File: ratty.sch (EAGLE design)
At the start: 90 parts, among them IC2 L293DD, Q1 BS170, Q2 BS170, Q3 BS170, Q5 BS170, U1 ITG-32001:1

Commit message: latest changes
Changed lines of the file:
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@@
 <part name="S1" library="switch-ck" deviceset="L101-XX-X-MS" device=""/>
 <part name="AGND9" library="supply1" deviceset="AGND" device=""/>
-<part name="GND28" library="supply2" deviceset="DGND" device=""/>
 <part name="GND30" library="supply2" deviceset="DGND" device=""/>
 <part name="GND31" library="supply2" deviceset="DGND" device=""/>
@@
 <part name="SUPPLY1" library="supply2" deviceset="DGND" device=""/>
 <part name="SUPPLY2" library="supply2" deviceset="DGND" device=""/>
+<part name="SUPPLY3" library="supply2" deviceset="DGND" device=""/>
 </parts>
 <sheets>
@@
 <instance part="S1" gate="G$1" x="43.18" y="114.3" rot="R90"/>
 <instance part="AGND9" gate="VR1" x="-93.98" y="213.36"/>
-<instance part="GND28" gate="G$1" x="-88.9" y="157.48"/>
 <instance part="GND30" gate="G$1" x="-50.8" y="157.48"/>
 <instance part="GND31" gate="G$1" x="-33.02" y="157.48"/>
@@
 <instance part="SUPPLY1" gate="G$1" x="30.48" y="53.34" rot="R270"/>
 <instance part="SUPPLY2" gate="G$1" x="-68.58" y="154.94"/>
+<instance part="SUPPLY3" gate="G$1" x="-88.9" y="154.94"/>
 </instances>
 <busses>
@@
 </segment>
 <segment>
-<pinref part="C11" gate="G$1" pin="2"/>
-<wire x1="-88.9" y1="167.64" x2="-88.9" y2="160.02" width="0.1524" layer="91"/>
-<pinref part="GND28" gate="G$1" pin="DGND"/>
-</segment>
-<segment>
 <pinref part="C17" gate="G$1" pin="2"/>
 <pinref part="GND30" gate="G$1" pin="DGND"/>
@@
 <pinref part="SUPPLY2" gate="G$1" pin="DGND"/>
 </segment>
-</net>
+<segment>
+<pinref part="C11" gate="G$1" pin="2"/>
+<wire x1="-88.9" y1="167.64" x2="-88.9" y2="157.48" width="0.1524" layer="91"/>
+<pinref part="SUPPLY3" gate="G$1" pin="DGND"/>
+</segment>
+</net>

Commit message: Changed schematic a bit to make it easier to route
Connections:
- removed net PA_0_ENCODER1_1: U$4.PA0-TIM2_CH1/TIM2_ET/TIM5_CH1, U$8.L_CHA
- removed net PA_1_ENCODER1_2: U$4.PA1-TIM2_CH2/TIM5_CH2/SPI4_MOSI/I2S4_SD, U$8.L_CHB
- removed net PA_5_ENCODER2_1: U$4.PA5-TIM2_CH1/TIM2_ET/SPI1_SCK/I2S1_CK, U$8.R_CHA
- removed net PB3_ENCODER2_2: U$4.PB3-JTDO-SWO/TIME2_CH2/SPI1_SCK/SPI3_SCK/USART1_RX/I2C2_SDA, U$8.R_CHB
- removed net PB7_I2CSDA_FOR_GYRO: U$4.PB7-TIM4_CH2/I2C1_SDA/USART1_RX/SDIO_D0, U1.SDA
- removed net PB8_I2C1SCL_FOR_GYRO: U$4.PB8-TIM4_CH3/TIM10_CH1/I2C1_SCL/SPI5_MOSI/I2C3_SDA, U1.SCL
- removed net PB9_GYROCLK: U$4.PB9-TIM4_CH4/TIM11_CH11/I2C1_SDA/SPI2_NSS/I2C2_SDA, U1.CLKIN
- new net ENCODER1_1: U$4.PA5-TIM2_CH1/TIM2_ET/SPI1_SCK/I2S1_CK, U$8.L_CHA
- new net ENCODER1_2: U$4.PB3-JTDO-SWO/TIME2_CH2/SPI1_SCK/SPI3_SCK/USART1_RX/I2C2_SDA, U$8.L_CHB
- new net ENCODER2_1: U$4.PA0-TIM2_CH1/TIM2_ET/TIM5_CH1, U$8.R_CHA
- new net ENCODER2_2: U$4.PA1-TIM2_CH2/TIM5_CH2/SPI4_MOSI/I2S4_SD, U$8.R_CHB
- new net GYROCLK: U$4.PA9-TIM1_CH2/I2C3_SMBA/USART1_TX/SDIO_D2, U1.CLKIN
- new net I2CSCL_FOR_GYRO: U$4.PA8-MCO_1/TIM1_CH1/I2C3_SCL/USART1_CK/SDIO_D1, U1.SCL
- new net I2CSDA_FOR_GYRO: U$4.PC9-MCO_2/TIM3)CH4/I2C3_SDA/SDIO_D1, U1.SDA
- net L_DIGITAL_IN_1: now also U$4.PB7-TIM4_CH2/I2C1_SDA/USART1_RX/SDIO_D0; no longer U$4.PA8-MCO_1/TIM1_CH1/I2C3_SCL/USART1_CK/SDIO_D1
- net L_DIGITAL_IN_2: now also U$4.PB8-TIM4_CH3/TIM10_CH1/I2C1_SCL/SPI5_MOSI/I2C3_SDA; no longer U$4.PA9-TIM1_CH2/I2C3_SMBA/USART1_TX/SDIO_D2
- net PC9_REC_CIRCUIT_4: now also U$4.PC12-SPI3_MOSI/I2S3_SD/SDIO_CK; no longer U$4.PC9-MCO_2/TIM3)CH4/I2C3_SDA/SDIO_D1
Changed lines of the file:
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@@
 </segment>
 <segment>
-<pinref part="U$4" gate="G$1" pin="PA9-TIM1_CH2/I2C3_SMBA/USART1_TX/SDIO_D2"/>
-<wire x1="200.66" y1="307.34" x2="210.82" y2="307.34" width="0.1524" layer="91"/>
-<label x="210.82" y="307.34" size="1.778" layer="95" xref="yes"/>
+<pinref part="U$4" gate="G$1" pin="PB8-TIM4_CH3/TIM10_CH1/I2C1_SCL/SPI5_MOSI/I2C3_SDA"/>
+<wire x1="200.66" y1="264.16" x2="205.74" y2="264.16" width="0.1524" layer="91"/>
+<label x="205.74" y="264.16" size="1.778" layer="95" xref="yes"/>
 </segment>
 </net>
@@
 </segment>
 <segment>
-<pinref part="U$4" gate="G$1" pin="PA8-MCO_1/TIM1_CH1/I2C3_SCL/USART1_CK/SDIO_D1"/>
-<wire x1="200.66" y1="309.88" x2="210.82" y2="309.88" width="0.1524" layer="91"/>
-<label x="210.82" y="309.88" size="1.778" layer="95" xref="yes"/>
+<pinref part="U$4" gate="G$1" pin="PB7-TIM4_CH2/I2C1_SDA/USART1_RX/SDIO_D0"/>
+<wire x1="200.66" y1="266.7" x2="208.28" y2="266.7" width="0.1524" layer="91"/>
+<label x="205.74" y="266.7" size="1.778" layer="95" xref="yes"/>
 </segment>
 </net>
@@
 </segment>
 </net>
-<net name="PA_0_ENCODER1_1" class="0">
-<segment>
-<label x="213.36" y="330.2" size="1.778" layer="95" xref="yes"/>
-<pinref part="U$4" gate="G$1" pin="PA0-TIM2_CH1/TIM2_ET/TIM5_CH1"/>
-<wire x1="200.66" y1="330.2" x2="213.36" y2="330.2" width="0.1524" layer="91"/>
-</segment>
-<segment>
-<pinref part="U$8" gate="G$1" pin="L_CHA"/>
-<wire x1="345.44" y1="-5.08" x2="345.44" y2="-15.24" width="0.1524" layer="91"/>
-<label x="345.44" y="-15.24" size="1.778" layer="95" rot="R270" xref="yes"/>
-</segment>
-</net>
-<net name="PA_1_ENCODER1_2" class="0">
-<segment>
-<wire x1="200.66" y1="327.66" x2="218.44" y2="327.66" width="0.1524" layer="91"/>
-<label x="218.44" y="327.66" size="1.778" layer="95" xref="yes"/>
-<pinref part="U$4" gate="G$1" pin="PA1-TIM2_CH2/TIM5_CH2/SPI4_MOSI/I2S4_SD"/>
-</segment>
-<segment>
-<pinref part="U$8" gate="G$1" pin="L_CHB"/>
-<wire x1="350.52" y1="-5.08" x2="350.52" y2="-15.24" width="0.1524" layer="91"/>
-<label x="350.52" y="-15.24" size="1.778" layer="95" rot="R270" xref="yes"/>
-</segment>
-</net>
 <net name="PA_6_REC_CIRCUIT_2" class="0">
 <segment>
@@
 </segment>
 </net>
-<net name="PB8_I2C1SCL_FOR_GYRO" class="0">
-<segment>
-<pinref part="U$4" gate="G$1" pin="PB8-TIM4_CH3/TIM10_CH1/I2C1_SCL/SPI5_MOSI/I2C3_SDA"/>
-<wire x1="200.66" y1="264.16" x2="205.74" y2="264.16" width="0.1524" layer="91"/>
-<label x="205.74" y="264.16" size="1.778" layer="95" xref="yes"/>
-</segment>
-<segment>
-<pinref part="U1" gate="G$1" pin="SCL"/>
-<wire x1="246.38" y1="157.48" x2="251.46" y2="157.48" width="0.1524" layer="91"/>
-<label x="251.46" y="157.48" size="1.778" layer="95" xref="yes"/>
-</segment>
-</net>
 <net name="PB_0_EMIT_CIRCUIT_3" class="0">
 <segment>
@@
 <label x="213.36" y="284.48" size="1.778" layer="95" xref="yes"/>
 <pinref part="U$4" gate="G$1" pin="PB0-TIM1_CH2N/TIM3_CH3/SPI5_SCK"/>
-</segment>
-</net>
-<net name="PB7_I2CSDA_FOR_GYRO" class="0">
-<segment>
-<pinref part="U$4" gate="G$1" pin="PB7-TIM4_CH2/I2C1_SDA/USART1_RX/SDIO_D0"/>
-<wire x1="200.66" y1="266.7" x2="208.28" y2="266.7" width="0.1524" layer="91"/>
-<label x="208.28" y="266.7" size="1.778" layer="95" xref="yes"/>
-</segment>
-<segment>
-<pinref part="U1" gate="G$1" pin="SDA"/>
-<wire x1="246.38" y1="160.02" x2="251.46" y2="160.02" width="0.1524" layer="91"/>
-<label x="251.46" y="160.02" size="1.778" layer="95" xref="yes"/>
-</segment>
-</net>
-<net name="PB9_GYROCLK" class="0">
-<segment>
-<pinref part="U$4" gate="G$1" pin="PB9-TIM4_CH4/TIM11_CH11/I2C1_SDA/SPI2_NSS/I2C2_SDA"/>
-<wire x1="200.66" y1="261.62" x2="208.28" y2="261.62" width="0.1524" layer="91"/>
-<label x="208.28" y="261.62" size="1.778" layer="95" xref="yes"/>
-</segment>
-<segment>
-<pinref part="U1" gate="G$1" pin="CLKIN"/>
-<wire x1="246.38" y1="144.78" x2="251.46" y2="144.78" width="0.1524" layer="91"/>
-<label x="251.46" y="144.78" size="1.778" layer="95" xref="yes"/>
 </segment>
 </net>
@@
 </segment>
 </net>
-<net name="PB3_ENCODER2_2" class="0">
-<segment>
-<pinref part="U$4" gate="G$1" pin="PB3-JTDO-SWO/TIME2_CH2/SPI1_SCK/SPI3_SCK/USART1_RX/I2C2_SDA"/>
-<wire x1="200.66" y1="276.86" x2="213.36" y2="276.86" width="0.1524" layer="91"/>
-<label x="213.36" y="276.86" size="1.778" layer="95" xref="yes"/>
-</segment>
-<segment>
-<pinref part="U$8" gate="G$1" pin="R_CHB"/>
-<wire x1="401.32" y1="-5.08" x2="401.32" y2="-15.24" width="0.1524" layer="91"/>
-<label x="401.32" y="-15.24" size="1.778" layer="95" rot="R270" xref="yes"/>
-</segment>
-</net>
 <net name="PA_7_REC_CIRCUIT_1" class="0">
 <segment>
@@
 </segment>
 </net>
-<net name="PA_5_ENCODER2_1" class="0">
-<segment>
-<pinref part="U$4" gate="G$1" pin="PA5-TIM2_CH1/TIM2_ET/SPI1_SCK/I2S1_CK"/>
-<wire x1="200.66" y1="317.5" x2="208.28" y2="317.5" width="0.1524" layer="91"/>
-<label x="208.28" y="317.5" size="1.778" layer="95" xref="yes"/>
-</segment>
-<segment>
-<pinref part="U$8" gate="G$1" pin="R_CHA"/>
-<wire x1="396.24" y1="-5.08" x2="396.24" y2="-15.24" width="0.1524" layer="91"/>
-<label x="396.24" y="-15.24" size="1.778" layer="95" rot="R270" xref="yes"/>
-</segment>
-</net>
 <net name="PC8_REC_CIRCUIT_3" class="0">
 <segment>
@@
 <net name="PC9_REC_CIRCUIT_4" class="0">
 <segment>
-<pinref part="U$4" gate="G$1" pin="PC9-MCO_2/TIM3)CH4/I2C3_SDA/SDIO_D1"/>
-<wire x1="58.42" y1="248.92" x2="55.88" y2="248.92" width="0.1524" layer="91"/>
-<label x="58.42" y="248.92" size="1.778" layer="95" rot="R180" xref="yes"/>
-</segment>
-<segment>
 <pinref part="U$13" gate="G$1" pin="E"/>
 <pinref part="R12" gate="G$1" pin="2"/>
@@
 <label x="586.74" y="134.62" size="1.778" layer="95" rot="R180" xref="yes"/>
 </segment>
+<segment>
+<pinref part="U$4" gate="G$1" pin="PC12-SPI3_MOSI/I2S3_SD/SDIO_CK"/>
+<wire x1="58.42" y1="241.3" x2="45.72" y2="241.3" width="0.1524" layer="91"/>
+<label x="45.72" y="241.3" size="1.778" layer="95" rot="R180" xref="yes"/>
+</segment>
 </net>
 <net name="RED_LED" class="0">
@@
 </segment>
 </net>
+<net name="I2CSCL_FOR_GYRO" class="0">
+<segment>
+<pinref part="U$4" gate="G$1" pin="PA8-MCO_1/TIM1_CH1/I2C3_SCL/USART1_CK/SDIO_D1"/>
+<wire x1="200.66" y1="309.88" x2="210.82" y2="309.88" width="0.1524" layer="91"/>
+<label x="210.82" y="309.88" size="1.778" layer="95" xref="yes"/>
+</segment>
+<segment>
+<pinref part="U1" gate="G$1" pin="SCL"/>
+<wire x1="246.38" y1="157.48" x2="251.46" y2="157.48" width="0.1524" layer="91"/>
+<label x="251.46" y="157.48" size="1.778" layer="95" xref="yes"/>
+</segment>
+</net>
+<net name="GYROCLK" class="0">
+<segment>
+<pinref part="U$4" gate="G$1" pin="PA9-TIM1_CH2/I2C3_SMBA/USART1_TX/SDIO_D2"/>
+<wire x1="200.66" y1="307.34" x2="210.82" y2="307.34" width="0.1524" layer="91"/>
+<label x="210.82" y="307.34" size="1.778" layer="95" xref="yes"/>
+</segment>
+<segment>
+<pinref part="U1" gate="G$1" pin="CLKIN"/>
+<wire x1="246.38" y1="144.78" x2="251.46" y2="144.78" width="0.1524" layer="91"/>
+<label x="251.46" y="144.78" size="1.778" layer="95" xref="yes"/>
+</segment>
+</net>
+<net name="I2CSDA_FOR_GYRO" class="0">
+<segment>
+<pinref part="U$4" gate="G$1" pin="PC9-MCO_2/TIM3)CH4/I2C3_SDA/SDIO_D1"/>
+<wire x1="58.42" y1="248.92" x2="55.88" y2="248.92" width="0.1524" layer="91"/>
+<label x="58.42" y="248.92" size="1.778" layer="95" rot="R180" xref="yes"/>
+</segment>
+<segment>
+<pinref part="U1" gate="G$1" pin="SDA"/>
+<wire x1="246.38" y1="160.02" x2="251.46" y2="160.02" width="0.1524" layer="91"/>
+<label x="251.46" y="160.02" size="1.778" layer="95" xref="yes"/>
+</segment>
+</net>
+<net name="ENCODER2_1" class="0">
+<segment>
+<label x="213.36" y="330.2" size="1.778" layer="95" xref="yes"/>
+<pinref part="U$4" gate="G$1" pin="PA0-TIM2_CH1/TIM2_ET/TIM5_CH1"/>
+<wire x1="200.66" y1="330.2" x2="213.36" y2="330.2" width="0.1524" layer="91"/>
+</segment>
+<segment>
+<pinref part="U$8" gate="G$1" pin="R_CHA"/>
+<wire x1="396.24" y1="-5.08" x2="396.24" y2="-15.24" width="0.1524" layer="91"/>
+<label x="396.24" y="-15.24" size="1.778" layer="95" rot="R270" xref="yes"/>
+</segment>
+</net>
+<net name="ENCODER2_2" class="0">
+<segment>
+<wire x1="200.66" y1="327.66" x2="218.44" y2="327.66" width="0.1524" layer="91"/>
+<label x="218.44" y="327.66" size="1.778" layer="95" xref="yes"/>
+<pinref part="U$4" gate="G$1" pin="PA1-TIM2_CH2/TIM5_CH2/SPI4_MOSI/I2S4_SD"/>
+</segment>
+<segment>
+<pinref part="U$8" gate="G$1" pin="R_CHB"/>
+<wire x1="401.32" y1="-5.08" x2="401.32" y2="-15.24" width="0.1524" layer="91"/>
+<label x="401.32" y="-15.24" size="1.778" layer="95" rot="R270" xref="yes"/>
+</segment>
+</net>
+<net name="ENCODER1_1" class="0">
+<segment>
+<pinref part="U$4" gate="G$1" pin="PA5-TIM2_CH1/TIM2_ET/SPI1_SCK/I2S1_CK"/>
+<wire x1="200.66" y1="317.5" x2="208.28" y2="317.5" width="0.1524" layer="91"/>
+<label x="208.28" y="317.5" size="1.778" layer="95" xref="yes"/>
+</segment>
+<segment>
+<pinref part="U$8" gate="G$1" pin="L_CHA"/>
+<wire x1="345.44" y1="-5.08" x2="345.44" y2="-15.24" width="0.1524" layer="91"/>
+<label x="345.44" y="-15.24" size="1.778" layer="95" rot="R270" xref="yes"/>
+</segment>
+</net>
+<net name="ENCODER1_2" class="0">
+<segment>
+<pinref part="U$4" gate="G$1" pin="PB3-JTDO-SWO/TIME2_CH2/SPI1_SCK/SPI3_SCK/USART1_RX/I2C2_SDA"/>
+<wire x1="200.66" y1="276.86" x2="213.36" y2="276.86" width="0.1524" layer="91"/>
+<label x="213.36" y="276.86" size="1.778" layer="95" xref="yes"/>
+</segment>
+<segment>
+<pinref part="U$8" gate="G$1" pin="L_CHB"/>
+<wire x1="350.52" y1="-5.08" x2="350.52" y2="-15.24" width="0.1524" layer="91"/>
+<label x="350.52" y="-15.24" size="1.778" layer="95" rot="R270" xref="yes"/>
+</segment>
+</net>

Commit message: Moved components around
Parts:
- removed C19, C30: 0.1uF, rcl:C-EUC0603
- removed C32: 4.7uF, rcl:C-EUC0603
- Q1, Q2, Q3, Q5: value BS170 -> MOSFET-NCHANNELBSS123LT1G; device transistor-small-signal:BS170 -> transistors:MOSFET-NCHANNELBSS123LT1G
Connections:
- net 3.3V: no longer C19.1, C30.1, C32.1
- net DGND: no longer C19.2, C30.2, C32.2

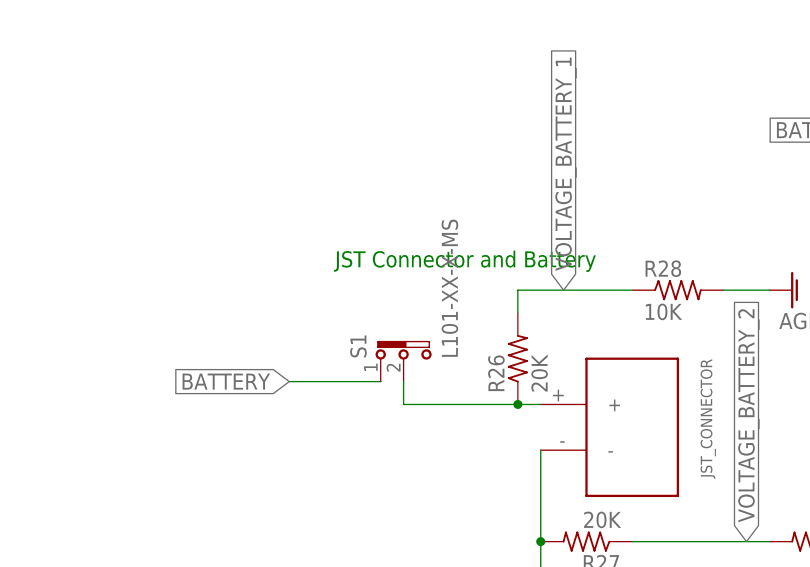
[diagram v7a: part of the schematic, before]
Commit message: Changed switch, resized, and added pours except AGND
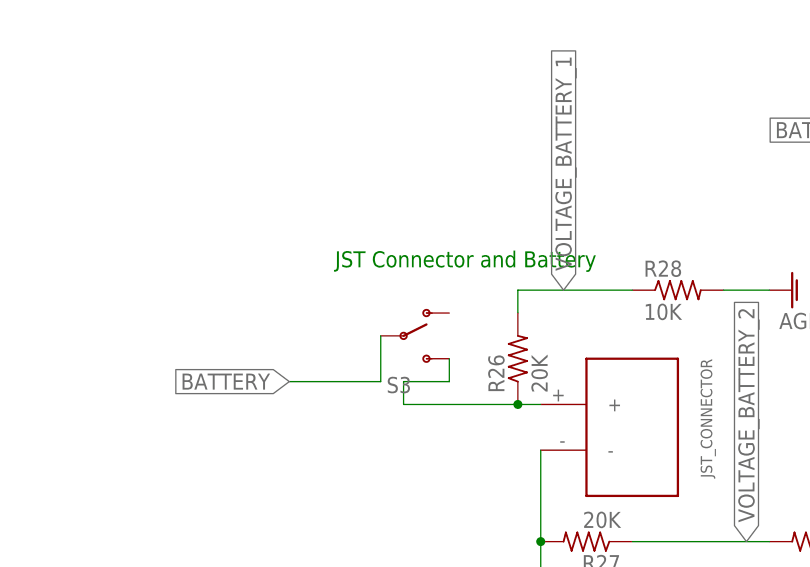
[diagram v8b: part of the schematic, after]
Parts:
- removed S1: L101-XX-X-MS, switch-ck:L101-XX-X-MS
- added S3: (no value), SparkFun:SWITCH-SPSTPTH
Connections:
- net BATTERY: now also S3.P; no longer S1.1
- net BATTERY_1: now also S3.S; no longer S1.2
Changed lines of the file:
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@@
 <?xml version="1.0" encoding="utf-8"?>
 <!DOCTYPE eagle SYSTEM "eagle.dtd">
-<eagle version="7.7.0">
+<eagle version="7.5.0">
 <drawing>
 <settings>
@@
 <part name="AGND8" library="supply1" deviceset="AGND" device=""/>
 <part name="GND27" library="SparkFun-Aesthetics" deviceset="DGND" device=""/>
-<part name="S1" library="switch-ck" deviceset="L101-XX-X-MS" device=""/>
 <part name="AGND9" library="supply1" deviceset="AGND" device=""/>
 <part name="GND30" library="supply2" deviceset="DGND" device=""/>
@@
 <part name="SUPPLY2" library="supply2" deviceset="DGND" device=""/>
 <part name="SUPPLY3" library="supply2" deviceset="DGND" device=""/>
+<part name="S3" library="SparkFun" deviceset="SWITCH-SPST" device="PTH"/>
 </parts>
 <sheets>
@@
 <instance part="AGND8" gate="VR1" x="99.06" y="93.98" rot="R90"/>
 <instance part="GND27" gate="G$1" x="213.36" y="236.22" rot="R90"/>
-<instance part="S1" gate="G$1" x="43.18" y="114.3" rot="R90"/>
 <instance part="AGND9" gate="VR1" x="-93.98" y="213.36"/>
 <instance part="GND30" gate="G$1" x="-50.8" y="157.48"/>
@@
 <instance part="SUPPLY2" gate="G$1" x="-68.58" y="154.94"/>
 <instance part="SUPPLY3" gate="G$1" x="-88.9" y="154.94"/>
+<instance part="S3" gate="1" x="43.18" y="116.84"/>
 </instances>
 <busses>
@@
 <wire x1="55.88" y1="109.22" x2="58.42" y2="109.22" width="0.1524" layer="91"/>
 <junction x="55.88" y="109.22"/>
-<pinref part="S1" gate="G$1" pin="2"/>
 <wire x1="43.18" y1="111.76" x2="43.18" y2="109.22" width="0.1524" layer="91"/>
+<pinref part="S3" gate="1" pin="S"/>
+<wire x1="48.26" y1="114.3" x2="48.26" y2="111.76" width="0.1524" layer="91"/>
+<wire x1="48.26" y1="111.76" x2="43.18" y2="111.76" width="0.1524" layer="91"/>
 </segment>
 </net>
@@
 <wire x1="30.48" y1="111.76" x2="40.64" y2="111.76" width="0.1524" layer="91"/>
 <label x="30.48" y="111.76" size="1.778" layer="95" rot="R180" xref="yes"/>
-<pinref part="S1" gate="G$1" pin="1"/>
-</segment>
-<segment>
+<pinref part="S3" gate="1" pin="P"/>
+<wire x1="40.64" y1="111.76" x2="40.64" y2="116.84" width="0.1524" layer="91"/>
+</segment>
+<segment>
